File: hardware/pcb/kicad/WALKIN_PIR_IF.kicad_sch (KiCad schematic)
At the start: 20 parts, among them J1 Battery Terminal, J2 XWA11V Terminal, J3 Probe Terminal, Q1 AO3401A, U1 AQY212EH

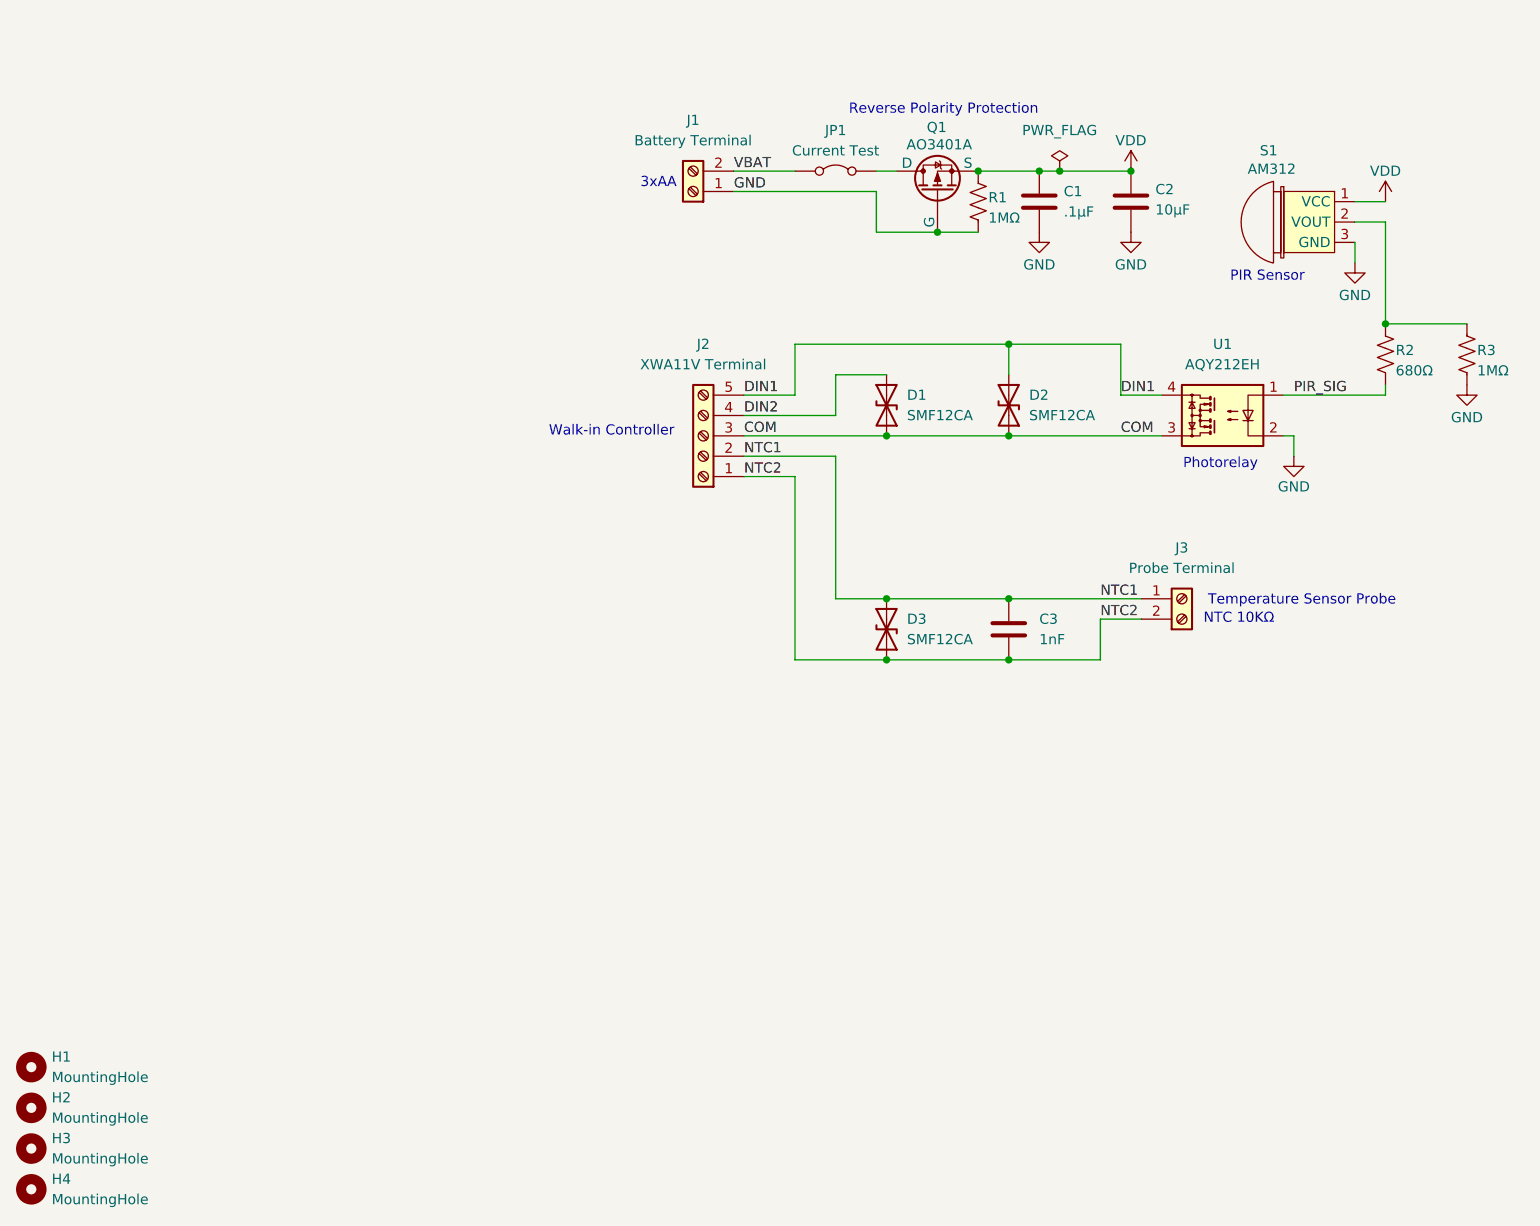
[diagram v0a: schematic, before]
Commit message: Added npn low side driver for photomos cathode for rev B
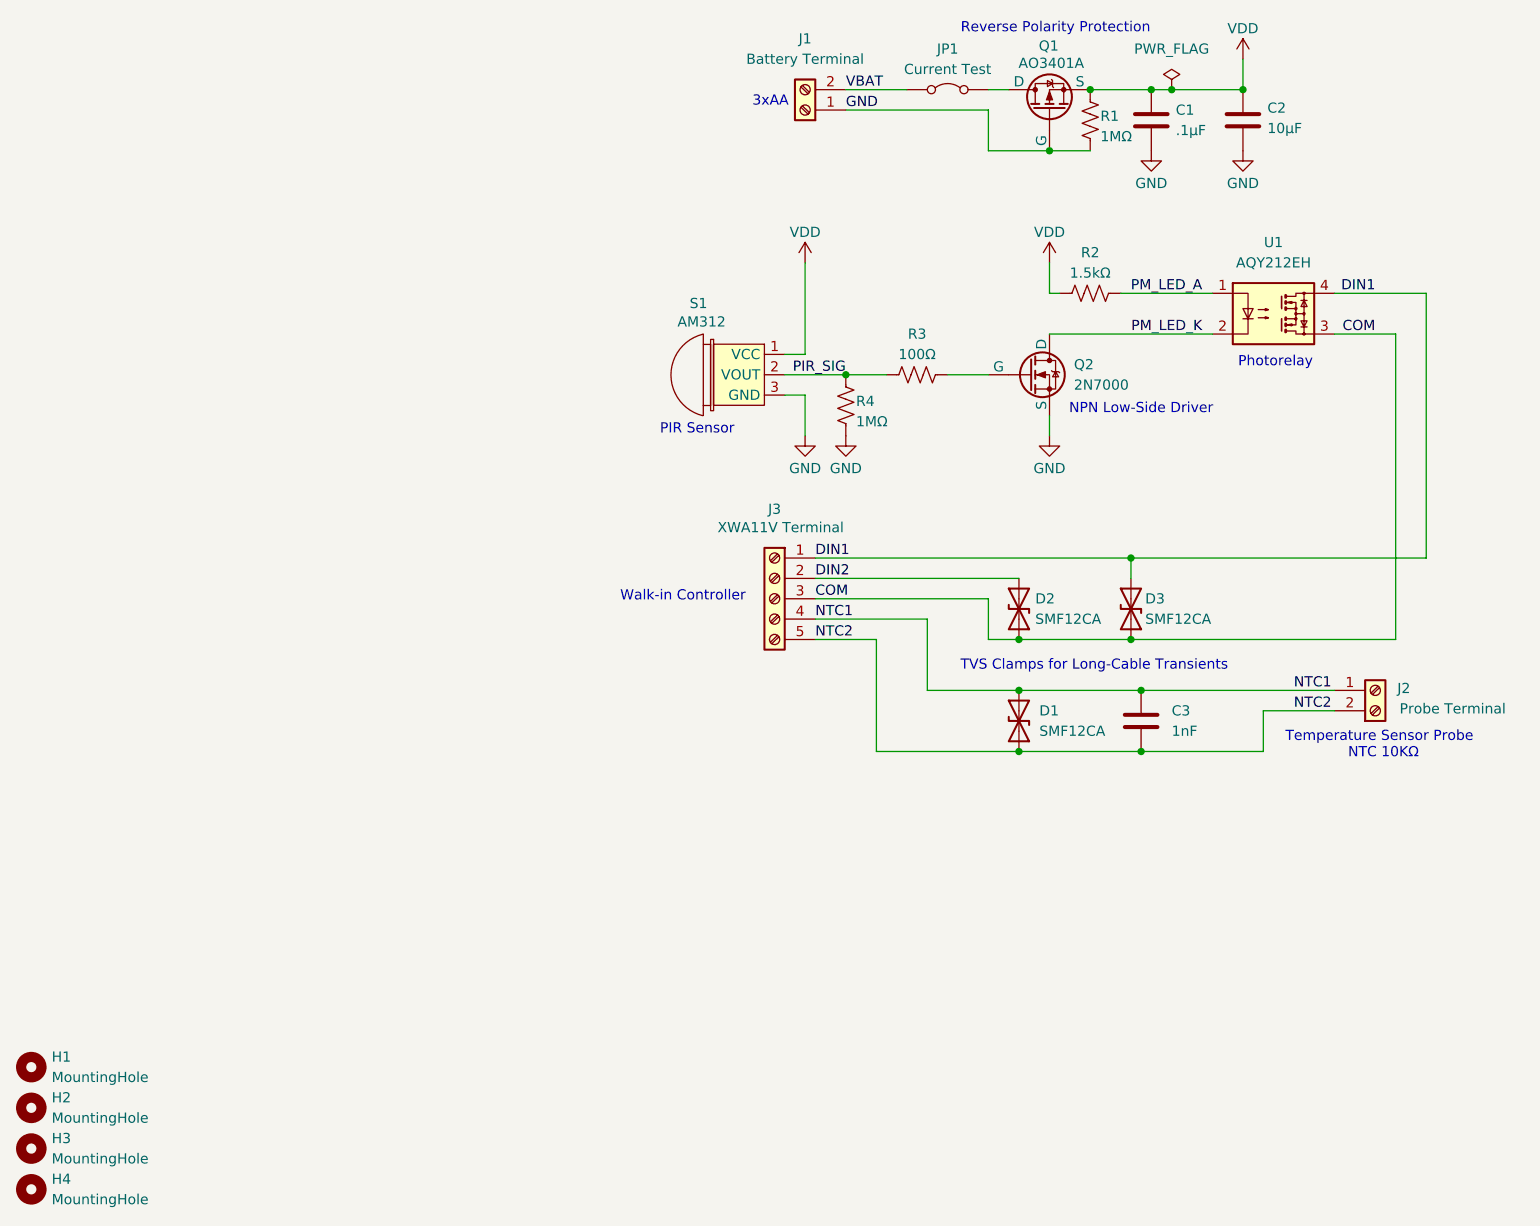
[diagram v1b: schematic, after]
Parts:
- added Q2: 2N7000, Package_TO_SOT_THT:TO-92_Inline, symbol Transistor_FET:2N7000
- added R3: 100Ω, Resistor_THT:R_Axial_DIN0207_L6.3mm_D2.5mm_P10.16mm_Horizontal, symbol Device:R_US
- R2: value 680Ω -> 1.5kΩ
- renumbered D3 to D1, D1 to D2, D2 to D3, J3 to J2, J2 to J3, R3 to R4
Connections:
- net DIN1: now also J3.1 (Pin_1); no longer J3.5 (Pin_5)
- net DIN2: now also J3.2 (Pin_2); no longer J3.4 (Pin_4)
- net GND: now also Q2.1 (S); no longer U1.2
- net NTC1: now also J3.4 (Pin_4); no longer J3.2 (Pin_2)
- net NTC2: now also J3.5 (Pin_5); no longer J3.1 (Pin_1)
- net PIR_SIG: now also R4.1, S1.2 (VOUT), R3.1; no longer R2.2, U1.1
- net VDD: now also R2.1
- new net: Q2.2 (G), R3.2
- new net PM_LED_A: R2.2, U1.1
- new net PM_LED_K: Q2.3 (D), U1.2
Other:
- note added: "NPN Low-Side Driver"
- note added: "TVS Clamps for Long-Cable Transients"
- moved on the sheet: C1, C2, C3, D1, D2, D3, J1, J2, J3, JP1, Q1, R1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

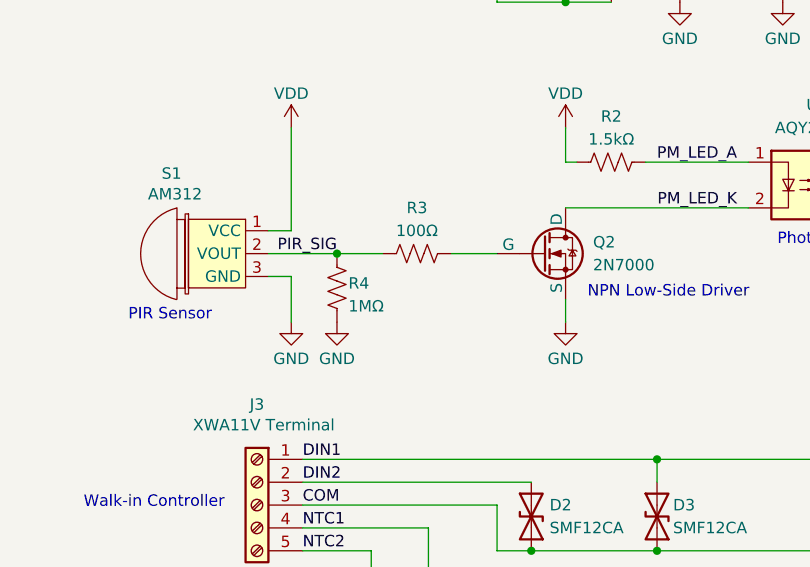
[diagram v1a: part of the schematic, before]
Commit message: moved pir pulldown r to npn gate and changed value to 100k
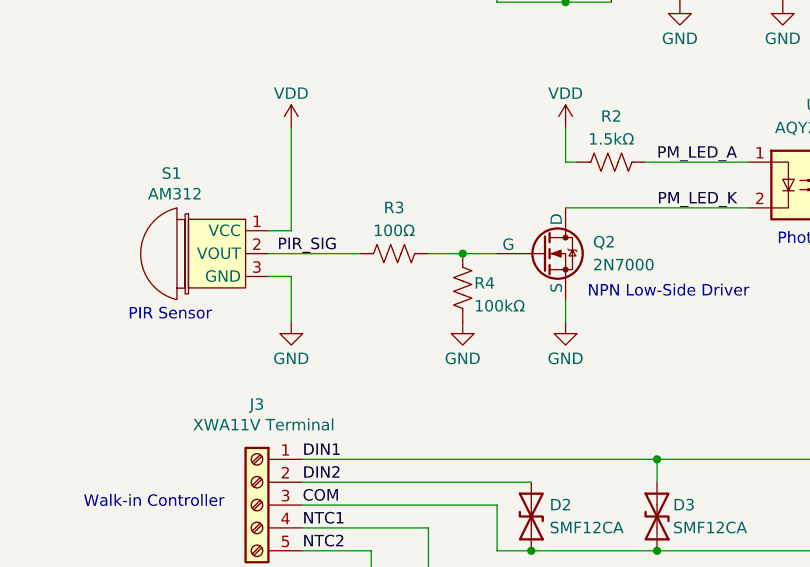
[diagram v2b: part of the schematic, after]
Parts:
- R4: value 1MΩ -> 100kΩ
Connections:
- net PIR_SIG: no longer R4.1
- net at Q2.2 (G), R3.2: now also R4.1
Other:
- moved on the sheet: R3, R4
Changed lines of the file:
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@@
-	)
-	(junction
-		(at 119.38 90.17)
-		(diameter 0)
-		(color 0 0 0 0)
 	)
 	(junction
@@
 	)
 	(junction
+		(at 133.35 90.17)
+		(diameter 0)
+		(color 0 0 0 0)
+	)
+	(junction
 		(at 156.21 129.54)
 		(diameter 0)
@@
 	(wire
 		(pts
-			(xy 124.46 90.17) (xy 119.38 90.17)
+			(xy 111.76 90.17) (xy 121.92 90.17)
 		)
 		(stroke
@@
 	(wire
 		(pts
-			(xy 132.08 90.17) (xy 137.16 90.17)
+			(xy 129.54 90.17) (xy 133.35 90.17)
 		)
 		(stroke
@@
 	(wire
 		(pts
-			(xy 111.76 90.17) (xy 119.38 90.17)
-		)
-		(stroke
-			(width 0)
-			(type default)
-		)
-	)
-	(wire
-		(pts
 			(xy 137.16 62.23) (xy 137.16 57.15)
+		)
+		(stroke
+			(width 0)
+			(type default)
+		)
+	)
+	(wire
+		(pts
+			(xy 133.35 90.17) (xy 137.16 90.17)
 		)
 		(stroke
@@
 	(symbol
 		(lib_id "power:GND")
-		(at 119.38 97.79 0)
+		(at 133.35 97.79 0)
 		(unit 1)
 		(exclude_from_sim no)
@@
 		(dnp no)
 		(property "Reference" "#PWR07"
-			(at 119.38 104.14 0)
+			(at 133.35 104.14 0)
 			(effects
 				(font
@@
 		)
 		(property "Value" "GND"
-			(at 119.38 101.854 0)
+			(at 133.35 101.854 0)
 			(effects
 				(font
@@
 		)
 		(property "Footprint" ""
-			(at 119.38 97.79 0)
+			(at 133.35 97.79 0)
 			(effects
 				(font
@@
 		)
 		(property "Datasheet" ""
-			(at 119.38 97.79 0)
+			(at 133.35 97.79 0)
 			(effects
 				(font
@@
 		)
 		(property "Description" "Power symbol creates a global label with name \"GND\" , ground"
-			(at 119.38 97.79 0)
+			(at 133.35 97.79 0)
 			(effects
 				(font
@@
 	(symbol
 		(lib_id "Device:R_US")
-		(at 119.38 93.98 0)
+		(at 133.35 93.98 0)
 		(unit 1)
 		(exclude_from_sim no)
@@
 		(dnp no)
 		(property "Reference" "R4"
-			(at 120.65 93.472 0)
+			(at 134.62 93.472 0)
 			(effects
 				(font
@@
 			)
 		)
-		(property "Value" "1MΩ"
-			(at 120.65 96.012 0)
+		(property "Value" "100kΩ"
+			(at 134.62 96.012 0)
 			(effects
 				(font
@@
 		)
 		(property "Footprint" "Resistor_THT:R_Axial_DIN0207_L6.3mm_D2.5mm_P10.16mm_Horizontal"
-			(at 120.396 94.234 90)
+			(at 134.366 94.234 90)
 			(effects
 				(font
@@
 		)
 		(property "Datasheet" "~"
-			(at 119.38 93.98 0)
+			(at 133.35 93.98 0)
 			(effects
 				(font
@@
 		)
 		(property "Description" "Resistor, US symbol"
-			(at 119.38 93.98 0)
+			(at 133.35 93.98 0)
 			(effects
 				(font
@@
 		)
 		(instances
-			(project "WALK_IN_SENSOR_REV_B"
+			(project "WALKIN_PIR_IF"
 				(path "/3a912c7a-047b-48d2-b4e3-d5db37149948"
 					(reference "R4")
@@
 	(symbol
 		(lib_id "Device:R_US")
-		(at 128.27 90.17 90)
+		(at 125.73 90.17 90)
 		(unit 1)
 		(exclude_from_sim no)
@@
 		(dnp no)
 		(property "Reference" "R3"
-			(at 128.27 85.09 90)
+			(at 125.73 85.09 90)
 			(effects
 				(font
@@
 		)
 		(property "Value" "100Ω"
-			(at 128.27 87.63 90)
+			(at 125.73 87.63 90)
 			(effects
 				(font
@@
 		)
 		(property "Footprint" "Resistor_THT:R_Axial_DIN0207_L6.3mm_D2.5mm_P10.16mm_Horizontal"
-			(at 128.524 89.154 90)
+			(at 125.984 89.154 90)
 			(effects
 				(font
@@
 		)
 		(property "Datasheet" "~"
-			(at 128.27 90.17 0)
+			(at 125.73 90.17 0)
 			(effects
 				(font
@@
 		)
 		(property "Description" "Resistor, US symbol"
-			(at 128.27 90.17 0)
-			(effects
-				(font
+			(at 125.73 90.17 0)
+			(effects
+				(font
